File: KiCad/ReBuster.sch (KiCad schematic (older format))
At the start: 11 parts, among them U3 SN74CBTD16210, U4 SN74LVC16T245DGVR, U5 SN74CBTD16210, U6 SN74CBTD16210, U7 74LVC2T45DC, U8 PLCC_84_plug, U9 PLCC_84_plug

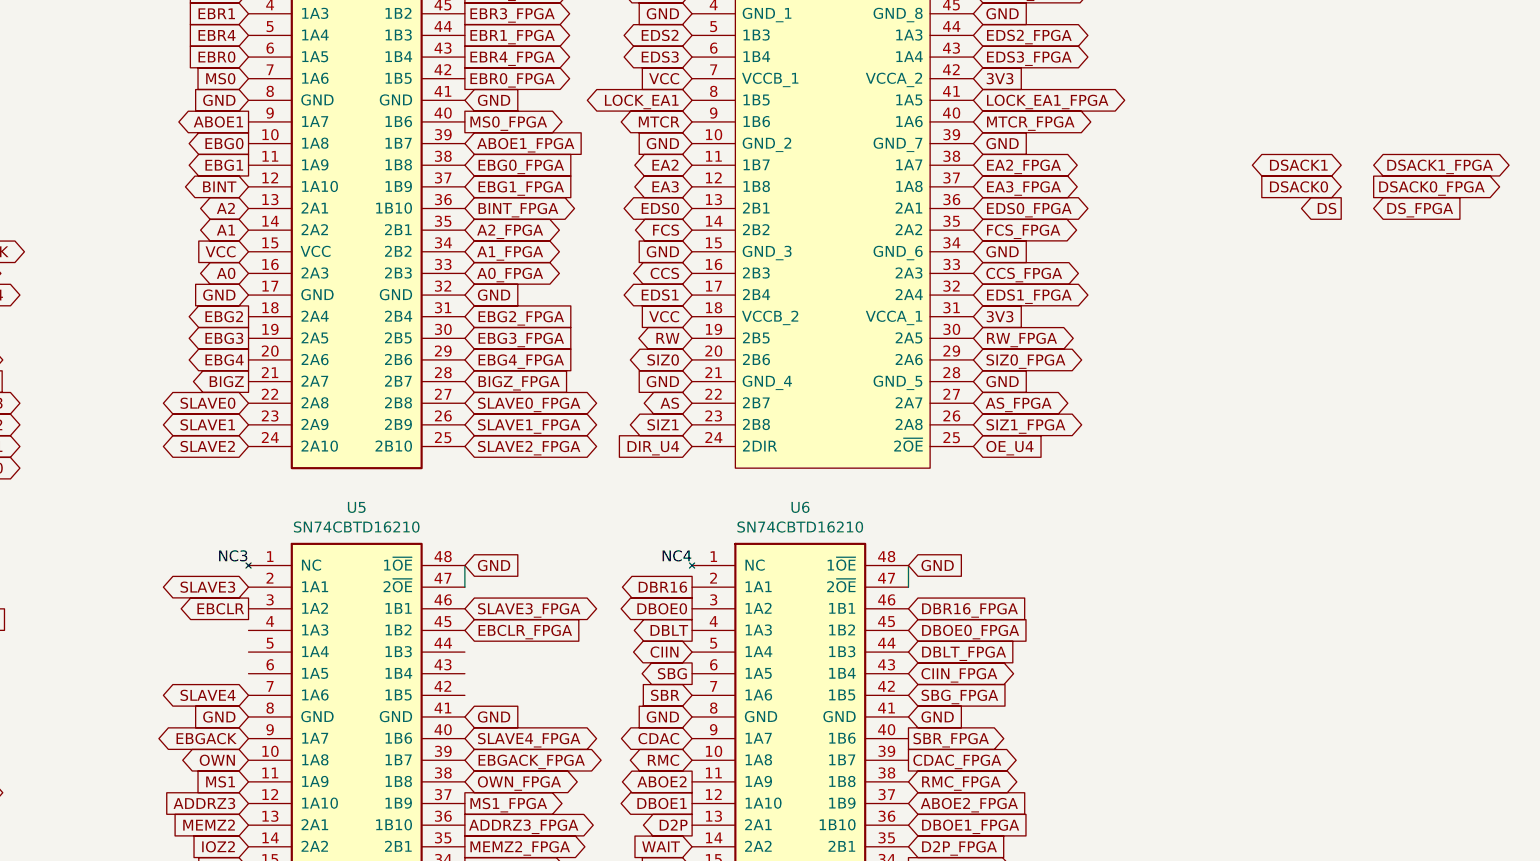
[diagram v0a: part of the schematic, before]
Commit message: small routing fixes upgrading 0.45/0.2 mm vias to 0.5/0.3 mm where possible
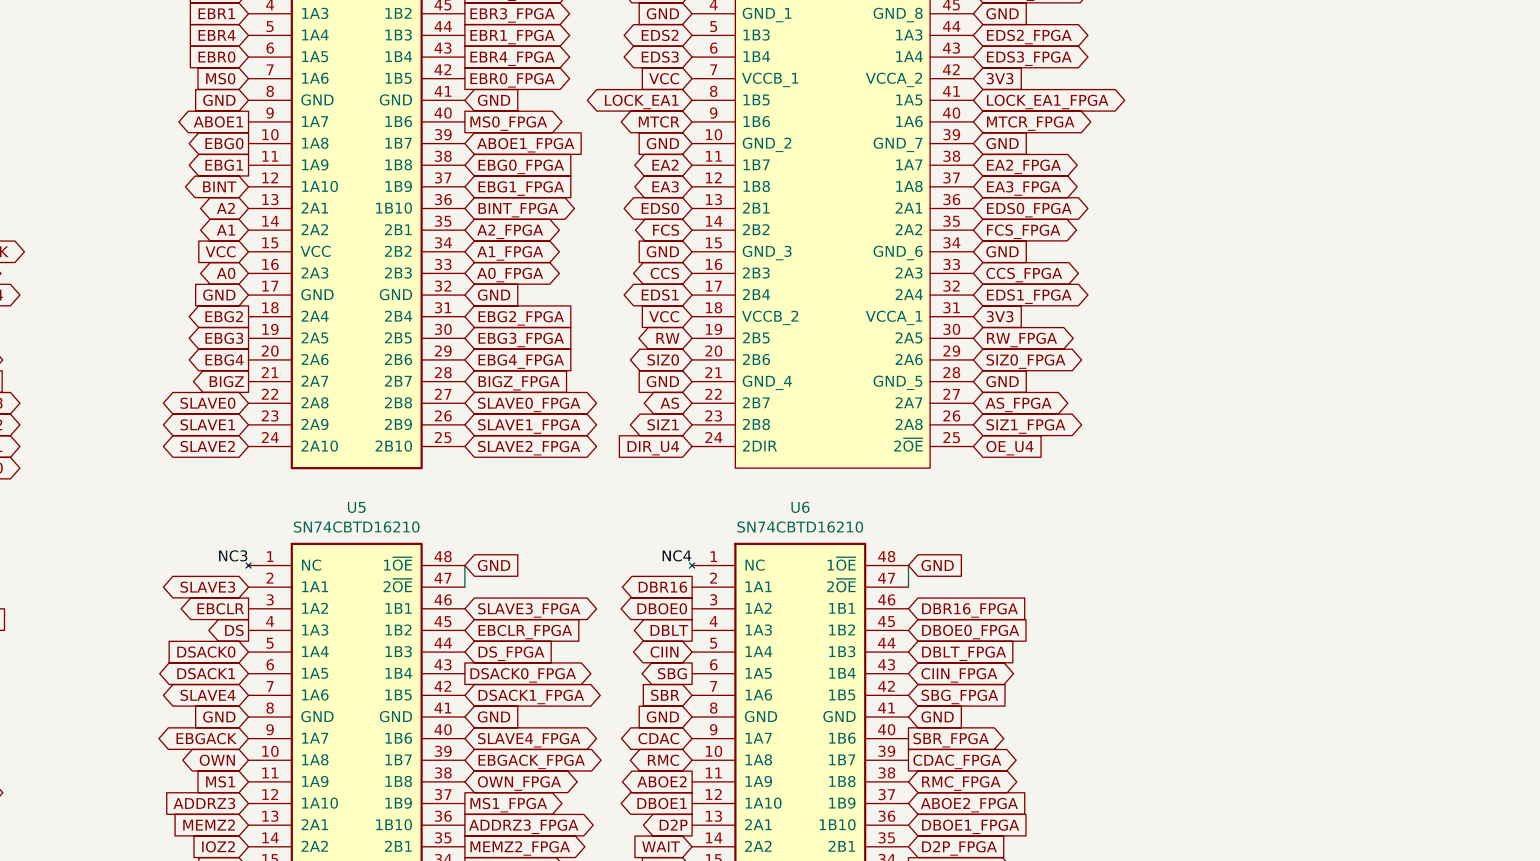
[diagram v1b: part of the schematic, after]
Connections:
- net DS: now also U5.4 (1A3)
- net DSACK0: now also U5.5 (1A4)
- net DSACK0_FPGA: now also U5.43 (1B4)
- net DSACK1: now also U5.6 (1A5)
- net DSACK1_FPGA: now also U5.42 (1B5)
- net DS_FPGA: now also U5.44 (1B3)
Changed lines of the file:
@@
 Text GLabel 8150 5800 2    50   BiDi ~ 0
 STERM_FPGA
-Text GLabel 12350 2150 2    50   Input ~ 0
+Text GLabel 8150 4200 2    50   Input ~ 0
 DS_FPGA
 Text GLabel 10500 3050 2    50   BiDi ~ 0
@@
 Text GLabel 9200 3050 0    50   BiDi ~ 0
 AS
-Text GLabel 12200 2150 0    50   Output ~ 0
+Text GLabel 7150 4100 0    50   Output ~ 0
 DS
-Text GLabel 12200 2050 0    50   Input ~ 0
+Text GLabel 7150 4200 0    50   Input ~ 0
 DSACK0
-Text GLabel 12200 1950 0    50   BiDi ~ 0
+Text GLabel 7150 4300 0    50   BiDi ~ 0
 DSACK1
 Text GLabel 7150 5800 0    50   BiDi ~ 0
@@
 Text GLabel 8150 2450 2    50   BiDi ~ 0
 A0_FPGA
-Text GLabel 12350 1950 2    50   BiDi ~ 0
+Text GLabel 8150 4400 2    50   BiDi ~ 0
 DSACK1_FPGA
-Text GLabel 12350 2050 2    50   Output ~ 0
+Text GLabel 8150 4300 2    50   Output ~ 0
 DSACK0_FPGA
 $Comp

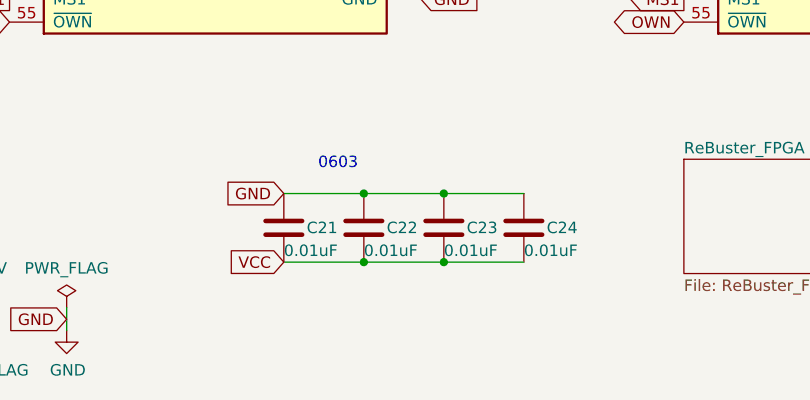
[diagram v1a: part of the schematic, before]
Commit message: Add VCC cap for U7 (74LVC2T45DC)
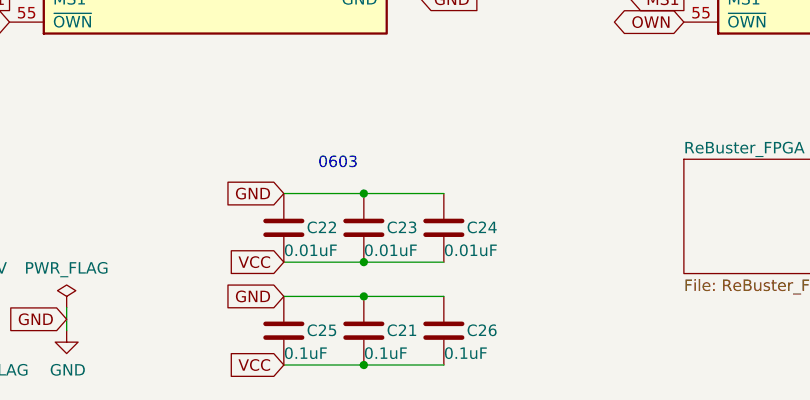
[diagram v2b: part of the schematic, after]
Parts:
- added C25: 0.1uF, ReBuster:C_0603_1608Metric_Pad1.05x0.95mm_HandSolder_extended, symbol Device:C
- added C26: 0.1uF, Capacitor_SMD:C_0603_1608Metric_Pad1.08x0.95mm_HandSolder, symbol Device:C
- C21: value 0.01uF -> 0.1uF
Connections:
- net +5V: now also C25.2, C26.2
- net GND: now also C25.1, C26.1
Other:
- moved on the sheet: C21, C22, C23, C24
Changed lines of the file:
@@
 Text GLabel 7150 2350 0    50   Input ~ 0
 VCC
-Connection ~ 2850 6850
-Connection ~ 2850 7150
 Wire Wire Line
 	10200 3900 10200 3800
@@
 Text GLabel 10200 6100 2    50   BiDi ~ 0
 BR_FPGA
-Wire Wire Line
-	2850 6850 3200 6850
-Wire Wire Line
-	2850 7150 3200 7150
 Text GLabel 2150 7150 0    50   Input ~ 0
 VCC
@@
 L Device:C C24
 U 1 1 605F0F7B
-P 3200 7000
-F 0 "C24" H 3300 7000 50  0000 L CNN
-F 1 "0.01uF" H 3200 6900 50  0000 L CNN
-F 2 "Capacitor_SMD:C_0603_1608Metric_Pad1.05x0.95mm_HandSolder" H 3238 6850 50  0001 C CNN
-F 3 "~" H 3200 7000 50  0001 C CNN
-	1    3200 7000
-	1    0    0    -1
-$EndComp
-$Comp
-L Device:C C23
-U 1 1 605D5D6F
 P 2850 7000
-F 0 "C23" H 2950 7000 50  0000 L CNN
+F 0 "C24" H 2950 7000 50  0000 L CNN
 F 1 "0.01uF" H 2850 6900 50  0000 L CNN
 F 2 "Capacitor_SMD:C_0603_1608Metric_Pad1.05x0.95mm_HandSolder" H 2888 6850 50  0001 C CNN
@@
 $EndComp
 $Comp
-L Device:C C22
-U 1 1 605D5659
+L Device:C C23
+U 1 1 605D5D6F
 P 2500 7000
-F 0 "C22" H 2600 7000 50  0000 L CNN
+F 0 "C23" H 2600 7000 50  0000 L CNN
 F 1 "0.01uF" H 2500 6900 50  0000 L CNN
 F 2 "Capacitor_SMD:C_0603_1608Metric_Pad1.05x0.95mm_HandSolder" H 2538 6850 50  0001 C CNN
@@
 $EndComp
 $Comp
-L Device:C C21
-U 1 1 605D3E60
+L Device:C C22
+U 1 1 605D5659
 P 2150 7000
-F 0 "C21" H 2250 7000 50  0000 L CNN
+F 0 "C22" H 2250 7000 50  0000 L CNN
 F 1 "0.01uF" H 2150 6900 50  0000 L CNN
 F 2 "Capacitor_SMD:C_0603_1608Metric_Pad1.05x0.95mm_HandSolder" H 2188 6850 50  0001 C CNN
 F 3 "~" H 2150 7000 50  0001 C CNN
 	1    2150 7000
+	1    0    0    -1
+$EndComp
+$Comp
+L Device:C C21
+U 1 1 605D3E60
+P 2500 7450
+F 0 "C21" H 2600 7450 50  0000 L CNN
+F 1 "0.1uF" H 2500 7350 50  0000 L CNN
+F 2 "Capacitor_SMD:C_0603_1608Metric_Pad1.05x0.95mm_HandSolder" H 2538 7300 50  0001 C CNN
+F 3 "~" H 2500 7450 50  0001 C CNN
+	1    2500 7450
 	1    0    0    -1
 $EndComp
@@
 	1    0    0    -1
 $EndComp
+$Comp
+L Device:C C25
+U 1 1 69EC0A34
+P 2150 7450
+F 0 "C25" H 2250 7450 50  0000 L CNN
+F 1 "0.1uF" H 2150 7350 50  0000 L CNN
+F 2 "ReBuster:C_0603_1608Metric_Pad1.05x0.95mm_HandSolder_extended" H 2188 7300 50  0001 C CNN
+F 3 "~" H 2150 7450 50  0001 C CNN
+	1    2150 7450
+	1    0    0    -1
+$EndComp
+Text GLabel 2150 7300 0    50   Input ~ 0
+GND
+Text GLabel 2150 7600 0    50   Input ~ 0
+VCC
+Wire Wire Line
+	2500 7300 2150 7300
+Wire Wire Line
+	2500 7600 2150 7600
+$Comp
+L Device:C C26
+U 1 1 69EC70AB
+P 2850 7450
+F 0 "C26" H 2950 7450 50  0000 L CNN
+F 1 "0.1uF" H 2850 7350 50  0000 L CNN
+F 2 "Capacitor_SMD:C_0603_1608Metric_Pad1.08x0.95mm_HandSolder" H 2888 7300 50  0001 C CNN
+F 3 "~" H 2850 7450 50  0001 C CNN
+	1    2850 7450
+	1    0    0    -1
+$EndComp
+Wire Wire Line
+	2500 7300 2850 7300
+Connection ~ 2500 7300
+Wire Wire Line
+	2500 7600 2850 7600
+Connection ~ 2500 7600
 $EndSCHEMATC

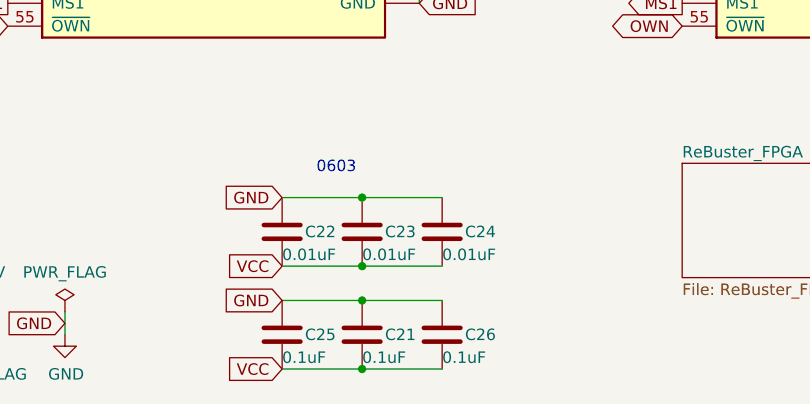
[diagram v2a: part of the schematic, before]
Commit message: Silkscreen fixes
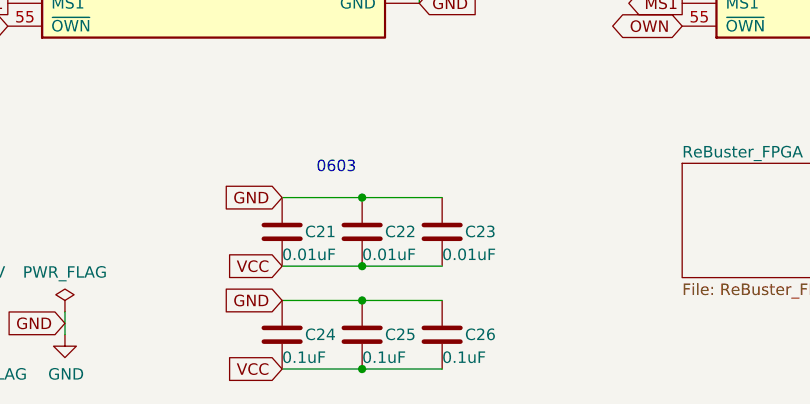
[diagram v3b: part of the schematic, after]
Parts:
- renumbered C22 to C21, C23 to C22, C24 to C23, C25 to C24, C21 to C25
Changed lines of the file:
@@
 0603
 $Comp
-L Device:C C24
+L Device:C C23
 U 1 1 605F0F7B
 P 2850 7000
-F 0 "C24" H 2950 7000 50  0000 L CNN
+F 0 "C23" H 2950 7000 50  0000 L CNN
 F 1 "0.01uF" H 2850 6900 50  0000 L CNN
 F 2 "Capacitor_SMD:C_0603_1608Metric_Pad1.05x0.95mm_HandSolder" H 2888 6850 50  0001 C CNN
@@
 $EndComp
 $Comp
-L Device:C C23
+L Device:C C22
 U 1 1 605D5D6F
 P 2500 7000
-F 0 "C23" H 2600 7000 50  0000 L CNN
+F 0 "C22" H 2600 7000 50  0000 L CNN
 F 1 "0.01uF" H 2500 6900 50  0000 L CNN
 F 2 "Capacitor_SMD:C_0603_1608Metric_Pad1.05x0.95mm_HandSolder" H 2538 6850 50  0001 C CNN
@@
 $EndComp
 $Comp
-L Device:C C22
+L Device:C C21
 U 1 1 605D5659
 P 2150 7000
-F 0 "C22" H 2250 7000 50  0000 L CNN
+F 0 "C21" H 2250 7000 50  0000 L CNN
 F 1 "0.01uF" H 2150 6900 50  0000 L CNN
 F 2 "Capacitor_SMD:C_0603_1608Metric_Pad1.05x0.95mm_HandSolder" H 2188 6850 50  0001 C CNN
@@
 $EndComp
 $Comp
-L Device:C C21
+L Device:C C25
 U 1 1 605D3E60
 P 2500 7450
-F 0 "C21" H 2600 7450 50  0000 L CNN
+F 0 "C25" H 2600 7450 50  0000 L CNN
 F 1 "0.1uF" H 2500 7350 50  0000 L CNN
 F 2 "Capacitor_SMD:C_0603_1608Metric_Pad1.05x0.95mm_HandSolder" H 2538 7300 50  0001 C CNN
@@
 $EndComp
 $Comp
-L Device:C C25
+L Device:C C24
 U 1 1 69EC0A34
 P 2150 7450
-F 0 "C25" H 2250 7450 50  0000 L CNN
+F 0 "C24" H 2250 7450 50  0000 L CNN
 F 1 "0.1uF" H 2150 7350 50  0000 L CNN
 F 2 "ReBuster:C_0603_1608Metric_Pad1.05x0.95mm_HandSolder_extended" H 2188 7300 50  0001 C CNN

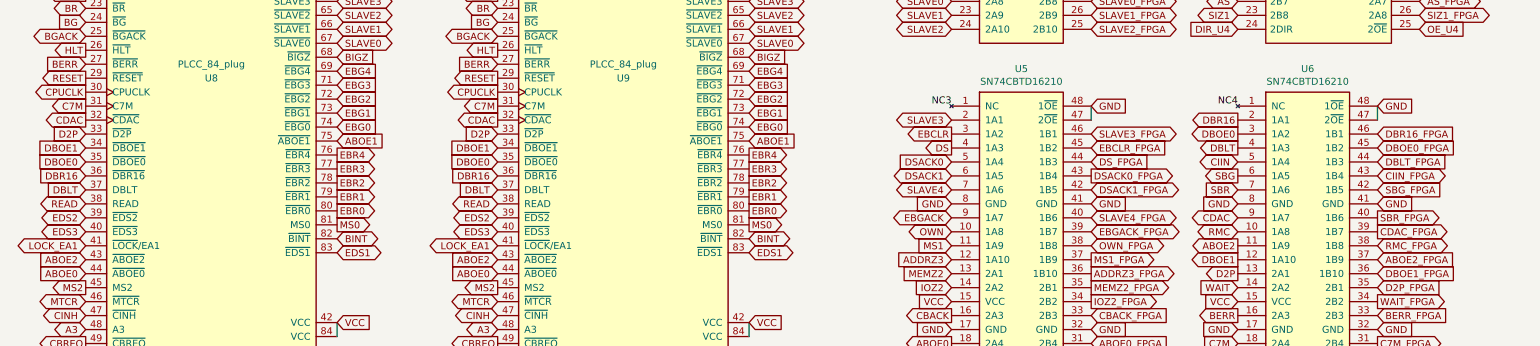
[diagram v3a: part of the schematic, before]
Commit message: remove CDAC clock (not used) and put /MTCR signal there
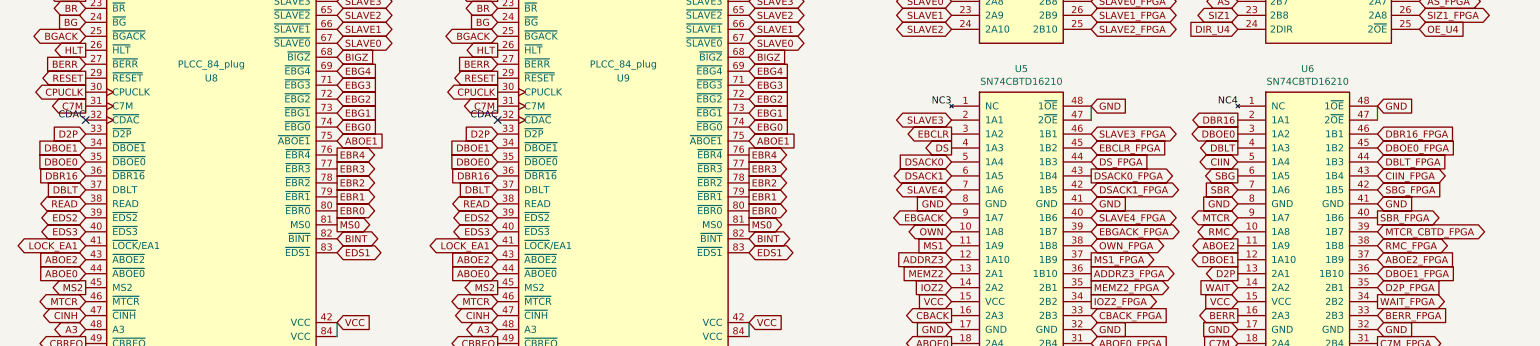
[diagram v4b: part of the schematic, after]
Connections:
- net CDAC: no longer U6.9 (1A7)
- net MTCR: now also U6.9 (1A7)
- net CDAC_FPGA renamed MTCR_CBTD_FPGA
- no-connect marks 0 -> 2
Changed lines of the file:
@@
 Text GLabel 10500 1450 2    50   BiDi ~ 0
 EDS3_FPGA
-Text GLabel 10200 4700 2    50   Output ~ 0
-CDAC_FPGA
 Text GLabel 10500 1650 2    50   BiDi ~ 0
 LOCK_EA1_FPGA
@@
 Text GLabel 950  3800 0    50   Output ~ 0
 C7M
-Text GLabel 950  3900 0    50   Output ~ 0
-CDAC
 Text GLabel 950  4000 0    50   Input ~ 0
 D2P
@@
 Text GLabel 9200 5500 0    50   Input ~ 0
 C7M
-Text GLabel 9200 4600 0    50   BiDi ~ 0
-CDAC
 Text GLabel 9200 5000 0    50   Output ~ 0
 D2P
@@
 Text GLabel 3900 3800 0    50   Output ~ 0
 C7M
-Text GLabel 3900 3900 0    50   Output ~ 0
-CDAC
 Text GLabel 3900 4000 0    50   Input ~ 0
 D2P
@@
 	2500 7600 2850 7600
 Connection ~ 2500 7600
+Text Label 3900 3900 2    50   ~ 0
+CDAC
+NoConn ~ 3900 3900
+Text Label 950  3900 2    50   ~ 0
+CDAC
+NoConn ~ 950  3900
+Text GLabel 10200 4700 2    50   BiDi ~ 0
+MTCR_CBTD_FPGA
+Text GLabel 9200 4600 0    50   BiDi ~ 0
+MTCR
 $EndSCHEMATC
